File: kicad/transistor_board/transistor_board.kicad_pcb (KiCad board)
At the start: 2 copper layers, 16 parts, among them J1 Conn_01x10, J2 Conn_01x02, Q1 MMBF170, Q2 MMBF170, Q3 MMBF170, Q4 MMBF170, U2 ESP32-cam, U3 LM7805_TO220

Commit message: working on PCB layout
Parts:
- moved Q4 61.4 mm to (119.4, 100.3)
- moved D2 58.7 mm to (125.7, 100.3)
- moved Q3 47.8 mm to (119.4, 106.7)
- moved Q2 47.7 mm to (132.1, 100.3), turned to 180 degrees
- moved Q1 45.3 mm to (132.1, 106.7), turned to 180 degrees
- moved R1 41.0 mm to (132.1, 117.2), turned to 90 degrees
- moved D3 40.2 mm to (125.7, 106.7), turned to 180 degrees
- moved D1 34.7 mm to (123.2, 116.8), turned to 180 degrees
- moved C3 28.8 mm to (132.1, 111.8), turned to 180 degrees
- moved C6 15.7 mm to (130.8, 123.2), turned to 180 degrees
- moved C5 12.0 mm to (133.3, 123.2), turned to 180 degrees
- moved C4 7.41 mm to (137.2, 121.9)
- moved U3 1.27 mm to (121.9, 130.8)
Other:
- board outline added: 25.4 x 40.6 mm

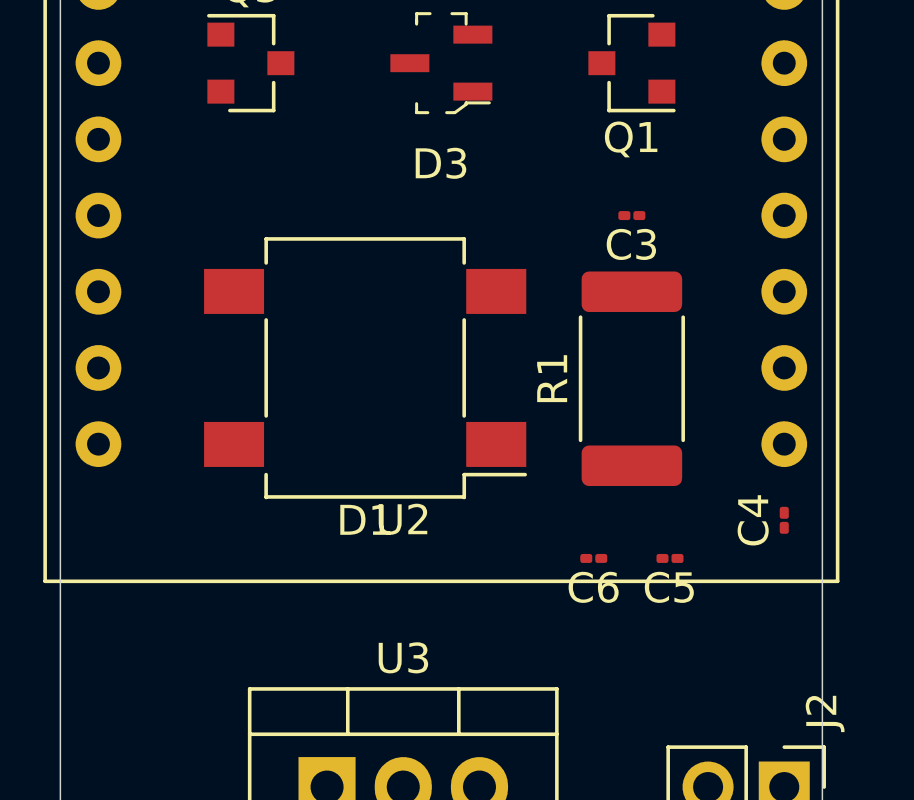
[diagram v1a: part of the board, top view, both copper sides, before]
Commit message: changed some footprints
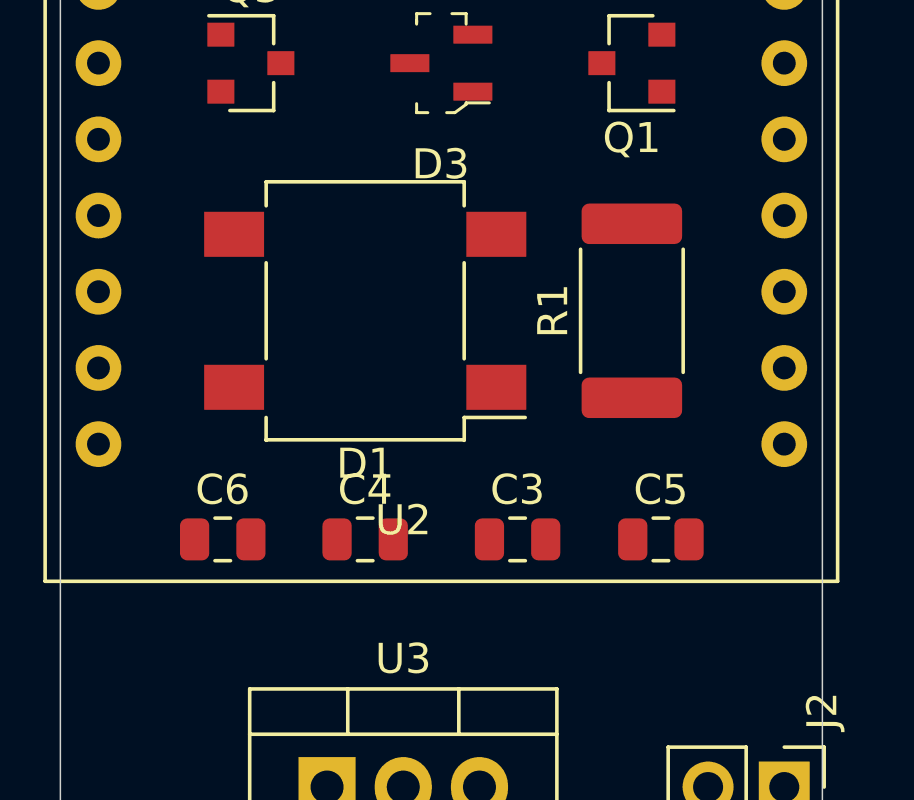
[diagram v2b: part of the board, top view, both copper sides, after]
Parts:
- C3, C4, C5, C6: footprint Capacitor_SMD:C_01005_0402Metric -> Capacitor_SMD:C_0805_2012Metric
- moved C4 14.0 mm to (123.2, 122.6), turned to 0 degrees
- moved C6 12.4 mm to (118.4, 122.6), turned to 0 degrees
- moved C3 11.4 mm to (128.3, 122.6), turned to 0 degrees
- moved R1 2.27 mm to (132.1, 114.9)
- moved D1 1.91 mm to (123.2, 114.9)
- moved C5 0.70 mm to (133.0, 122.6), turned to 0 degrees

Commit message: routed all
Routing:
- net GND: track 0.00 -> 119.5 mm
- net Net-(C3-Pad1): track 0.00 -> 79.1 mm, vias 0 -> 5
- net Net-(D2-Pad1): track 0.00 -> 52.9 mm, vias 0 -> 1
- net Net-(D2-Pad2): track 0.00 -> 51.1 mm
- net Net-(C6-Pad2): track 0.00 -> 50.0 mm, vias 0 -> 2
- net Net-(D3-Pad2): track 0.00 -> 46.8 mm, vias 0 -> 1
- net Net-(D3-Pad1): track 0.00 -> 40.0 mm, vias 0 -> 2
- net Net-(J2-Pad2): track 0.00 -> 32.2 mm
- net Net-(C5-Pad1): track 0.00 -> 31.4 mm
- net Net-(Q4-Pad1): track 0.00 -> 28.3 mm, vias 0 -> 1
- net Net-(D1-Pad3): track 0.00 -> 26.2 mm
- net Net-(C4-Pad1): track 0.00 -> 23.7 mm, vias 0 -> 1
- net Net-(D1-Pad4): track 0.00 -> 21.9 mm
- net Net-(Q3-Pad1): track 0.00 -> 20.5 mm, vias 0 -> 1
- net Net-(Q2-Pad1): track 0.00 -> 13.2 mm, vias 0 -> 1
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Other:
- board size 25.4 x 40.6 mm -> 26.4 x 40.6 mm

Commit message: some text on PCB
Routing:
- net GND: track 119.5 -> 118.2 mm
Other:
- board size 26.4 x 40.6 mm -> 25.9 x 40.6 mm
- board text added: "2020-08-02"
- board text added: "AC chassi"
- board text added: "AC shoe"
- board text added: "cap neg"
- board text added: "cap pos"
- board text added: "com"
- board text added: "lamps fwd"
- board text added: "lamps rev"
- board text added: "motor fwd"
- board text added: "motor rev"

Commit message: adjusting the PCB
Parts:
- moved U3 6.75 mm to (127.0, 126.4), turned to 180 degrees
- moved J2 5.12 mm to (134.6, 126.4), turned to 90 degrees
- moved J1 1.90 mm to (137.2, 134.0)
- turned C6 to 180 degrees
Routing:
- net Net-(J2-Pad2): track 32.2 -> 23.7 mm, vias 0 -> 2
- net Net-(C3-Pad1): track 79.1 -> 70.7 mm, vias 5 -> 4
- net Net-(D3-Pad1): track 40.0 -> 35.8 mm, vias 2 -> 1
- net Net-(D1-Pad4): track 21.9 -> 18.6 mm
- net GND: track 118.2 -> 121.2 mm
- net Net-(D2-Pad2): track 51.1 -> 49.2 mm
- net Net-(D1-Pad3): track 26.2 -> 24.4 mm
- net Net-(C5-Pad1): track 31.4 -> 29.8 mm, vias 0 -> 1
- net Net-(C4-Pad1): track 23.7 -> 22.6 mm
- net Net-(D2-Pad1): track 52.9 -> 51.9 mm
- net Net-(D3-Pad2): track 46.8 -> 45.9 mm
- net Net-(Q1-Pad1): track 8.36 -> 9.18 mm
- net Net-(C6-Pad2): track 50.0 -> 50.4 mm, vias 2 -> 1
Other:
- board size 25.9 x 40.6 mm -> 25.4 x 38.1 mm
- board text added: "Henrik & Johan Bjorkman www.drekkar.com 2020-08-03"
- board text removed: "2020-08-02"

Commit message: gerber files
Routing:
- net Net-(D3-Pad1): track 35.8 -> 39.8 mm
- net GND: track 121.2 -> 124.6 mm
- net Net-(D3-Pad2): track 45.9 -> 48.7 mm
- net Net-(C3-Pad1): track 70.7 -> 71.9 mm
- net Net-(Q3-Pad1): track 20.5 -> 21.1 mm
- added copper zone on F.Cu, net GND
- added copper zone on B.Cu, net Net-(C3-Pad1)

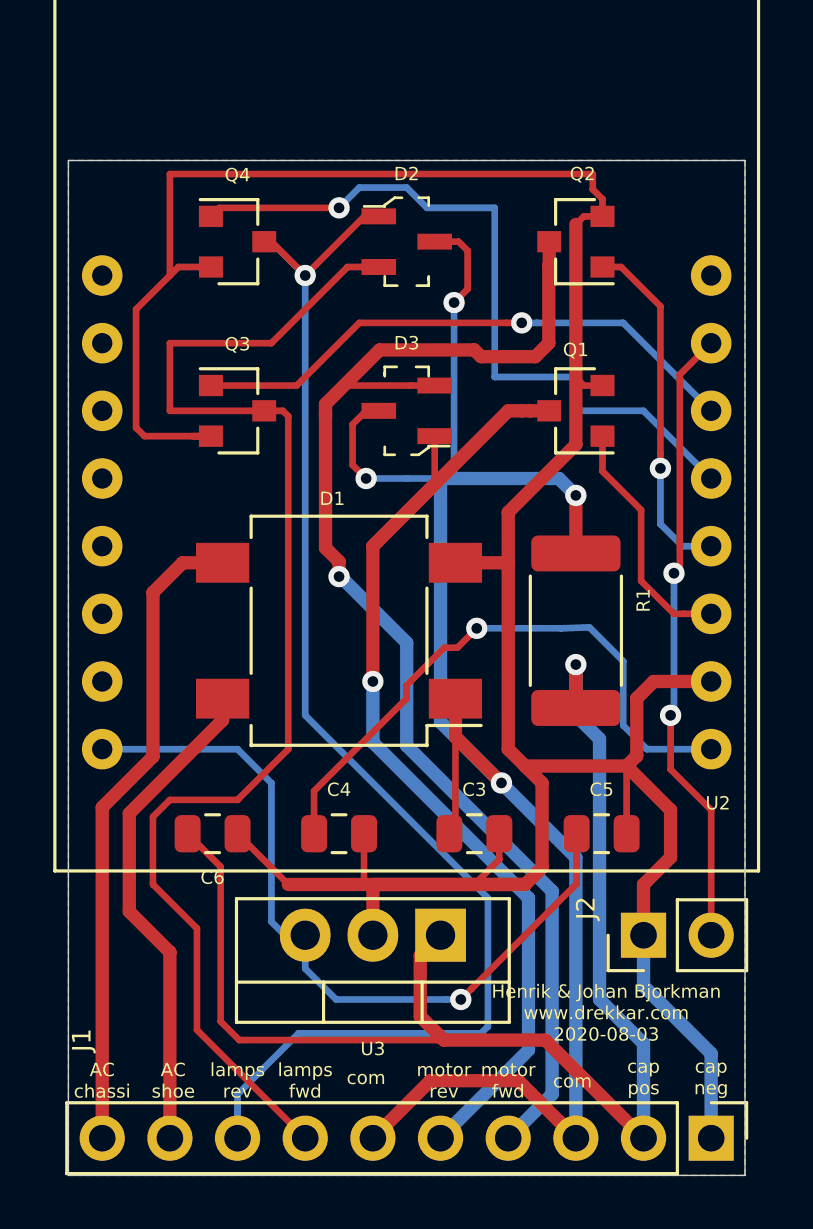
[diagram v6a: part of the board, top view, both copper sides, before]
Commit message: made cut out for connecting serial port
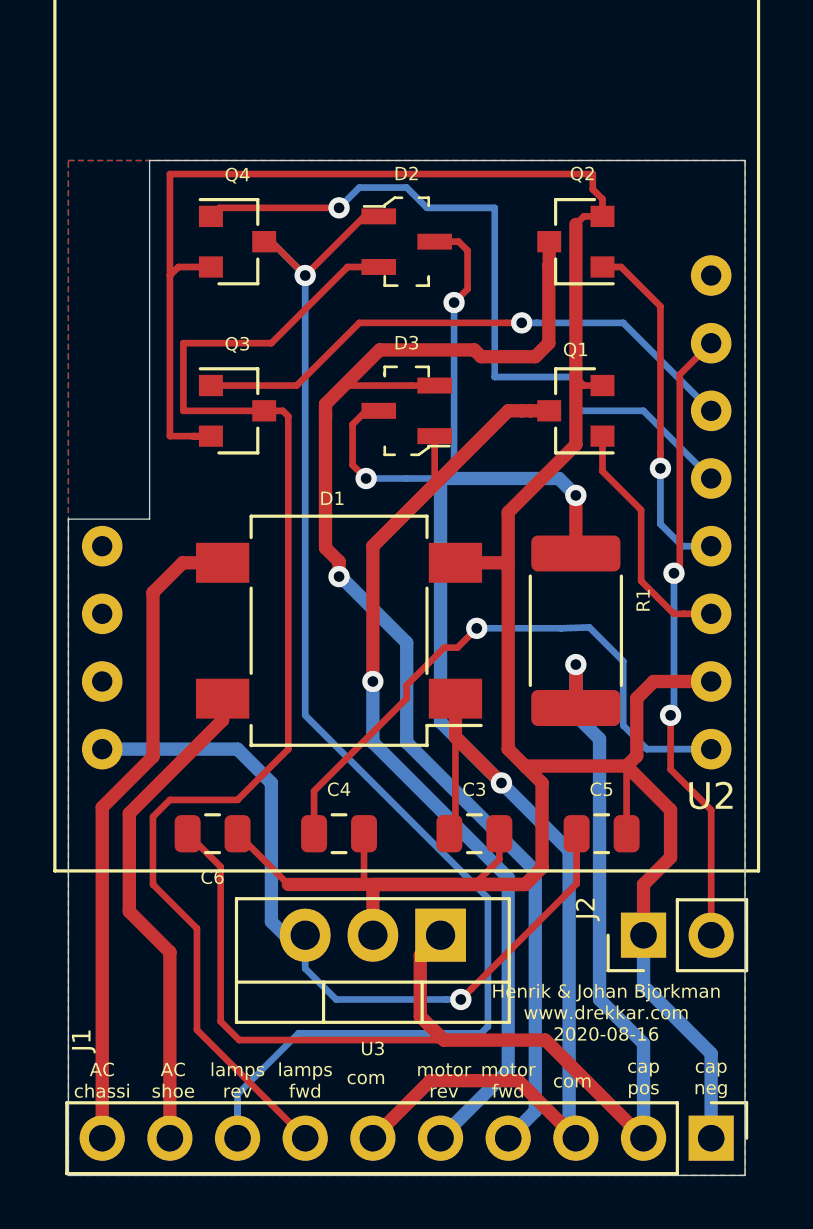
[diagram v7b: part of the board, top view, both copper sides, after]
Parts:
- U2: footprint transistor_board:ESP32-CAM -> eit_footprints:ESP32-CAM_12pin
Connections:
- U2 pad 13: Net-(U2-Pad13) -> GND
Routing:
- net Net-(C3-Pad1): track 71.9 -> 69.1 mm
- net GND: track 124.6 -> 123.0 mm
- net Net-(D2-Pad2): track 49.2 -> 48.1 mm
- net Net-(D3-Pad1): track 39.8 -> 39.2 mm
- net Net-(D3-Pad2): track 48.7 -> 48.2 mm
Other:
- outline, holes or cut-outs redrawn
- board text added: "Henrik & Johan Bjorkman www.drekkar.com 2020-08-16"
- board text removed: "Henrik & Johan Bjorkman www.drekkar.com 2020-08-03"

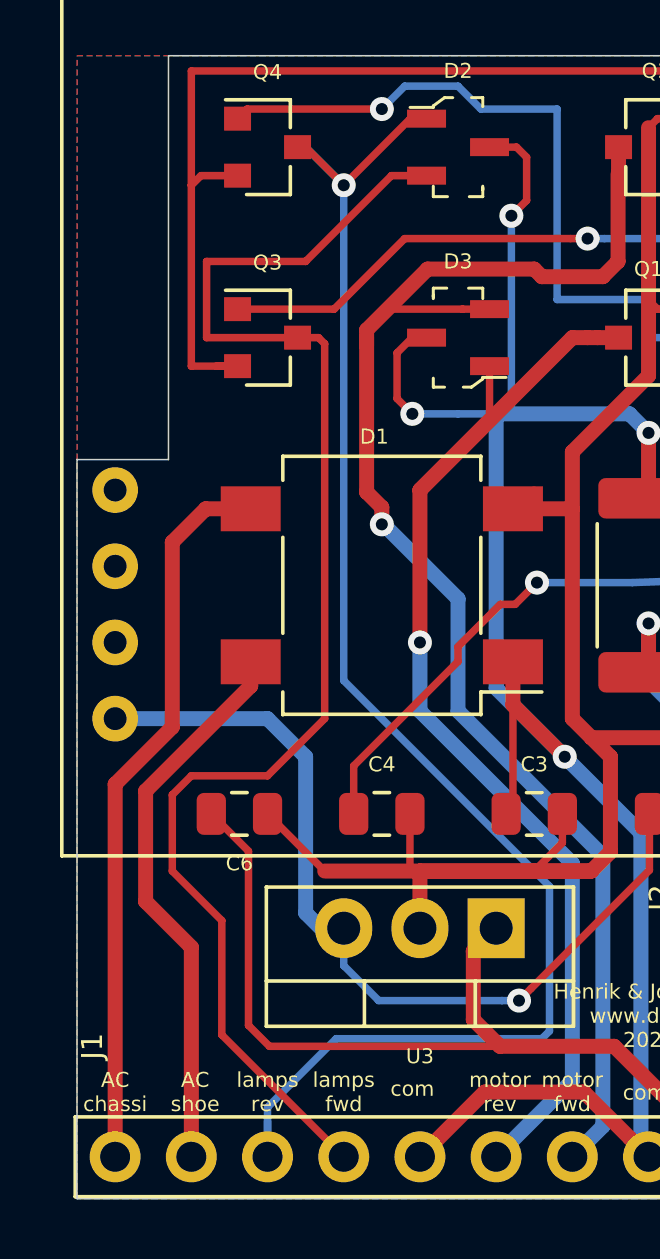
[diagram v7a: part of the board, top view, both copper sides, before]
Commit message: remember: To enable download connect GPIO0/IO0 to GND.
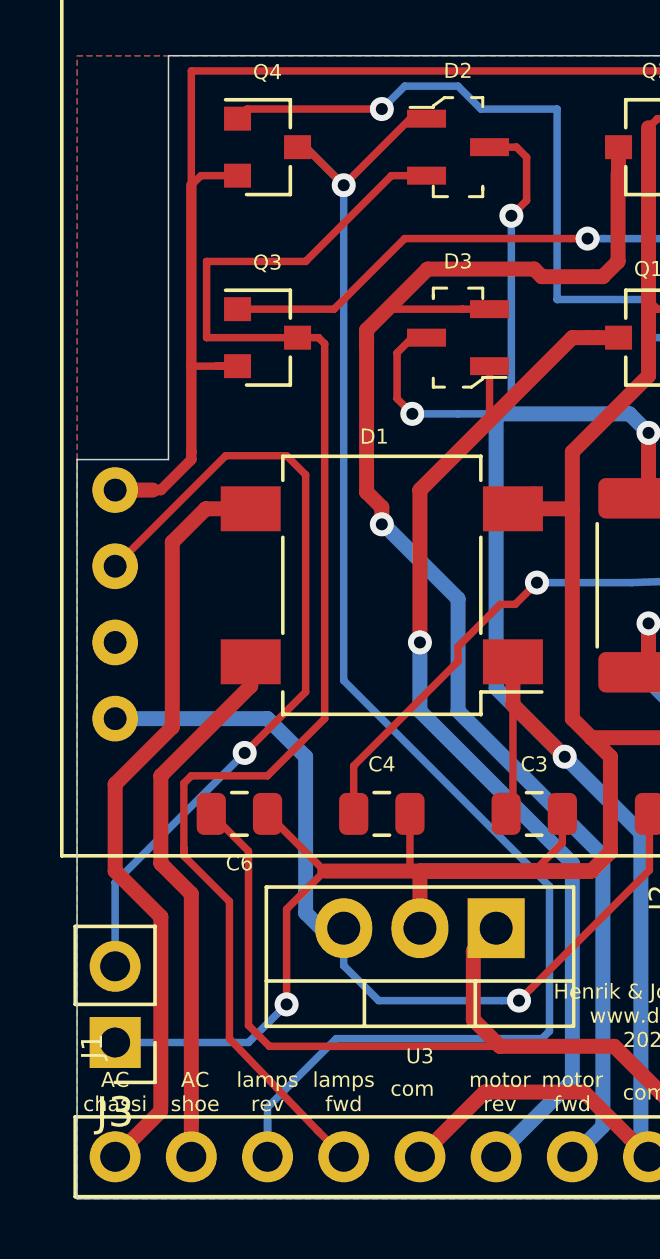
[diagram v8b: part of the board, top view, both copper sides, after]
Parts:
- added J3: Conn_01x02, Connector_PinHeader_2.54mm:PinHeader_1x02_P2.54mm_Vertical, F.Cu at (114.3, 130.2)
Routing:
- net Net-(J3-Pad2): track 0.00 -> 27.2 mm, vias 0 -> 1
- net GND: track 123.0 -> 140.3 mm, vias 0 -> 1
- net Net-(D1-Pad3): track 24.4 -> 25.7 mm
